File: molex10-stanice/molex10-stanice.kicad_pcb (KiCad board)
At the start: 2 copper layers, 90 x 52 mm, 19 parts, among them J1 MVE253-5-V, J10 MV132-3.5-V-L, J11 MV132-3.5-V-L, J12 MVE253-5-V, J13 MVE252-5-V, J14 MVE252-5-V, J15 MVE252-5-V, J2 TME 39281103 MOLEX, J3 MVE253-5-V, J4 MVE252-5-V, J5 MVE253-5-V, J6 TME 39281043 MOLEX, J7 RJ12, J8 MV132-3.5-V-L, J9 MV132-3.5-V-L

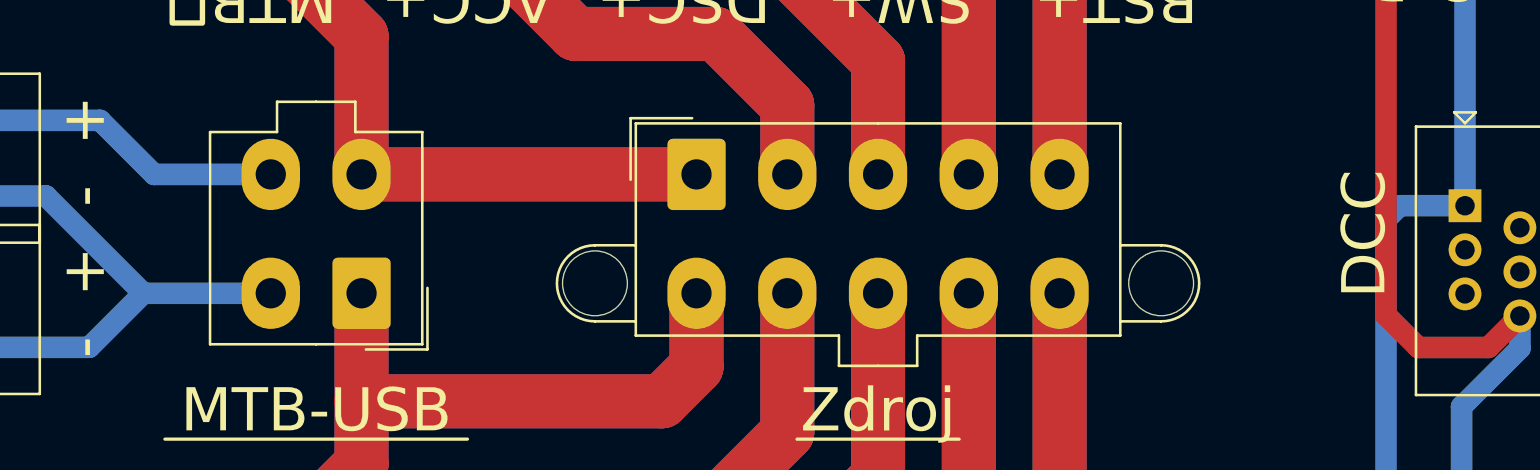
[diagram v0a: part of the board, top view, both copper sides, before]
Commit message: molex10-stanice: slight enhancements.
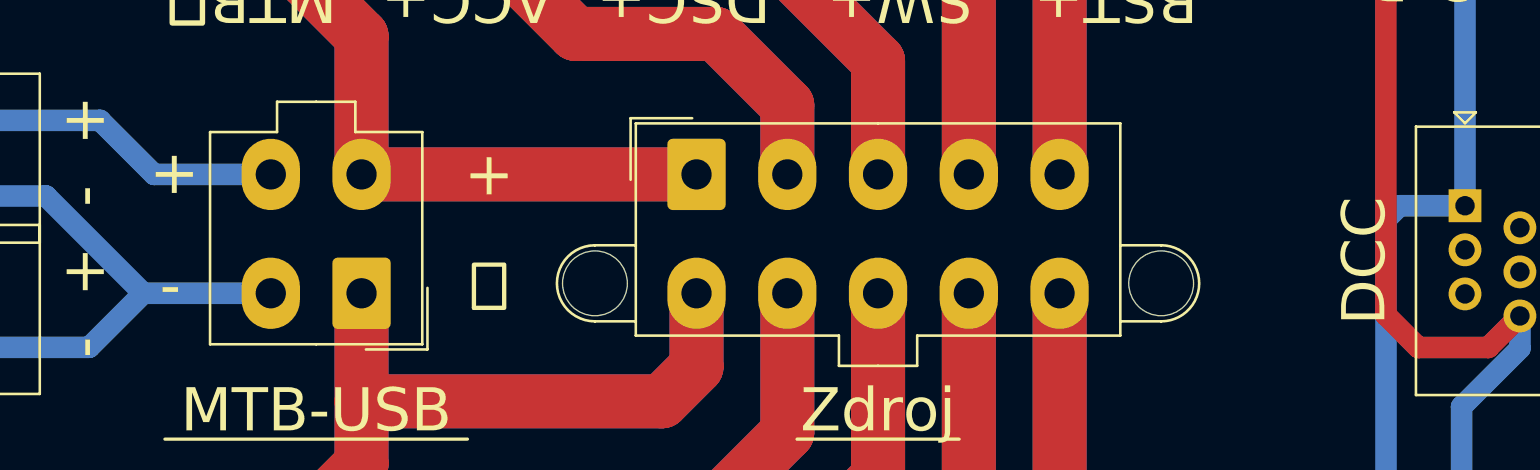
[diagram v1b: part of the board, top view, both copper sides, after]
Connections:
- net /BOOST- renamed /GND-BOOST
- net /DISC renamed /DSC
- net /GND renamed /GND-MTB
- net /GND2 renamed /GND-ACC
- net Net-(J14-Pin_1) renamed /GND-SWITCH
- net Net-(J2-Pin_8) renamed /GND-DSC
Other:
- board text added: "⏚"
